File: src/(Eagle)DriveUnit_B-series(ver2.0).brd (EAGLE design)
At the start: 65.7 x 51 mm, 55 parts, among them IC1 A3921, SW1 TVAF06-A020B-R, SW2 TVAF06-A020B-R, SW3 THAF01-NC-R, SW4 SS-12D00G3

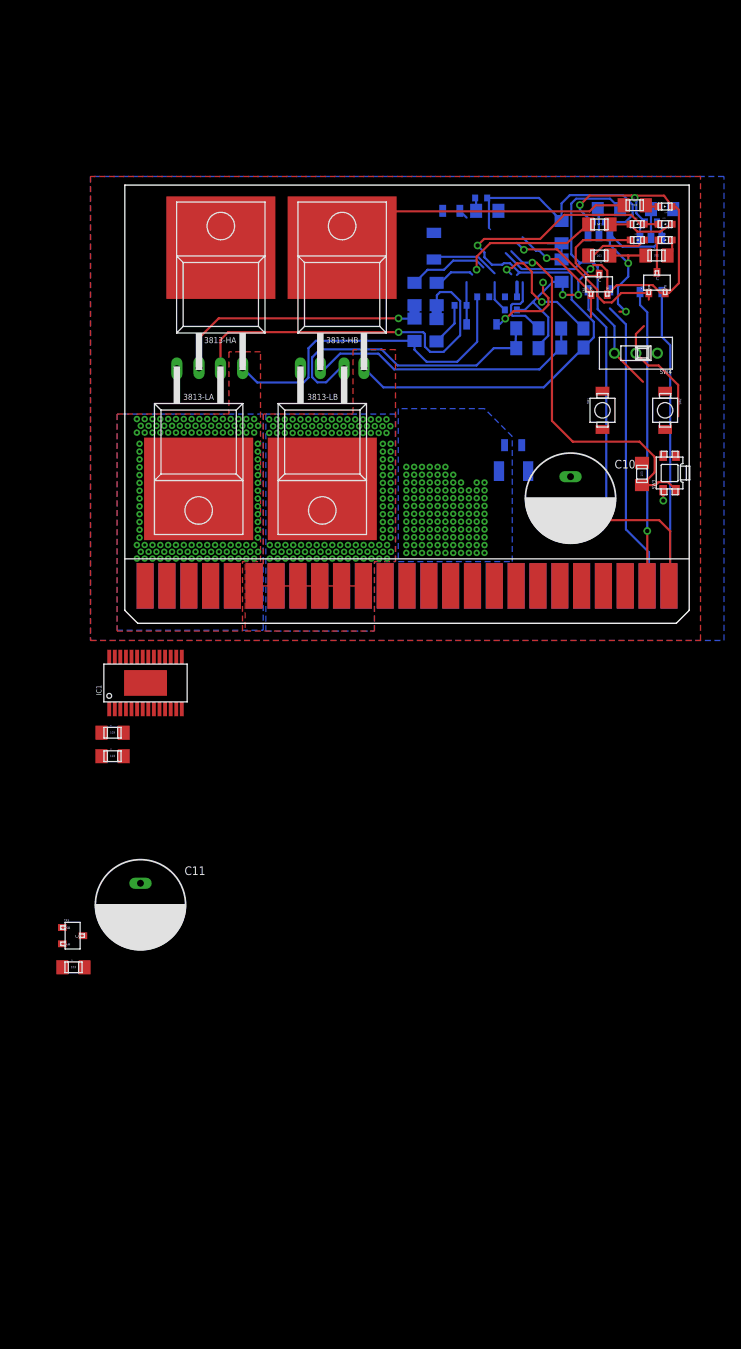
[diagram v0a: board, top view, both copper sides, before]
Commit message: 入力部分の追加
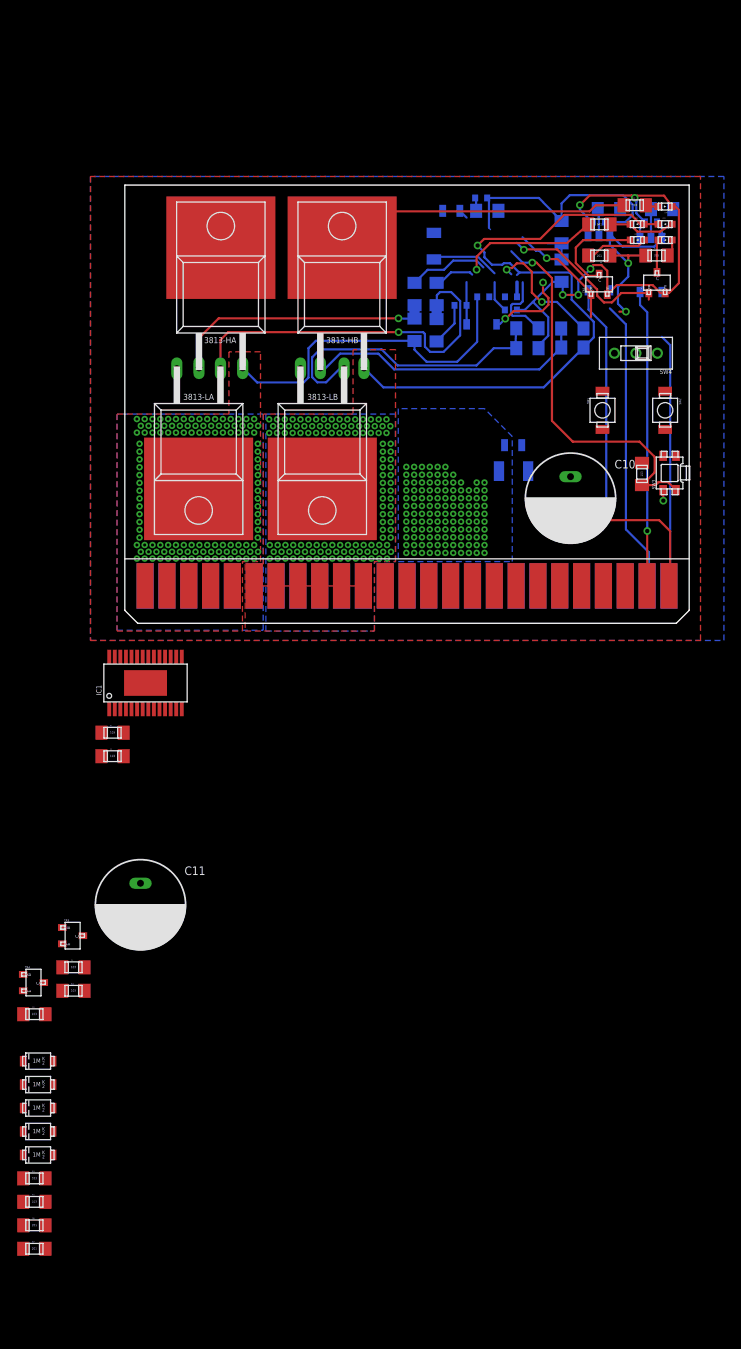
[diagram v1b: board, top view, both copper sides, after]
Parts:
- added D2, D3, D4, D5, D6: GS1010FL, GS1010FL:GS1010FL
- added R17, R23, R24, R25: RG2012, RG2012:RG2012
- added R26, R27: RG2012N-201-W-T1, RG2012N-201-W-T1:RG2012
- added TR4: 2SC3325, 2SC3325:2SC3325
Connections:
- new net LAP: D4.A, D5.A, R25.LEFT, R9.LEFT, SW4.C, TR3.B
- new net N$12: D3.A, R23.LEFT, TR4.C
- new net N$17: D4.C, R17.LEFT, R24.LEFT, SW1.RIGHT, TR4.B
- new net N$20: D5.C, D6.C, SW2.LEFT
- new net N$23: R26.LEFT, TLP1.1
- new net N$24: R27.LEFT, TLP2.1
- net DIR: now also D2.A, D2.C, D3.C, D6.A; no longer R9.LEFT, SW1.RIGHT, TR3.B
- net DIR_IN: now also R26.RIGHT; no longer TLP1.1
- net GND: now also R24.RIGHT, R25.RIGHT, SW2.RIGHT, SW4.R, TR4.E
- net PWM: no longer SW4.R
- net PWM_IN: now also R27.RIGHT; no longer TLP2.1
- net V5: now also R17.RIGHT, R23.RIGHT; no longer SW4.C
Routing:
- net PWM: track 41.4 -> 0.00 mm
- net V5: track 70.5 -> 56.9 mm
- net DIR_IN: track 34.7 -> 29.5 mm

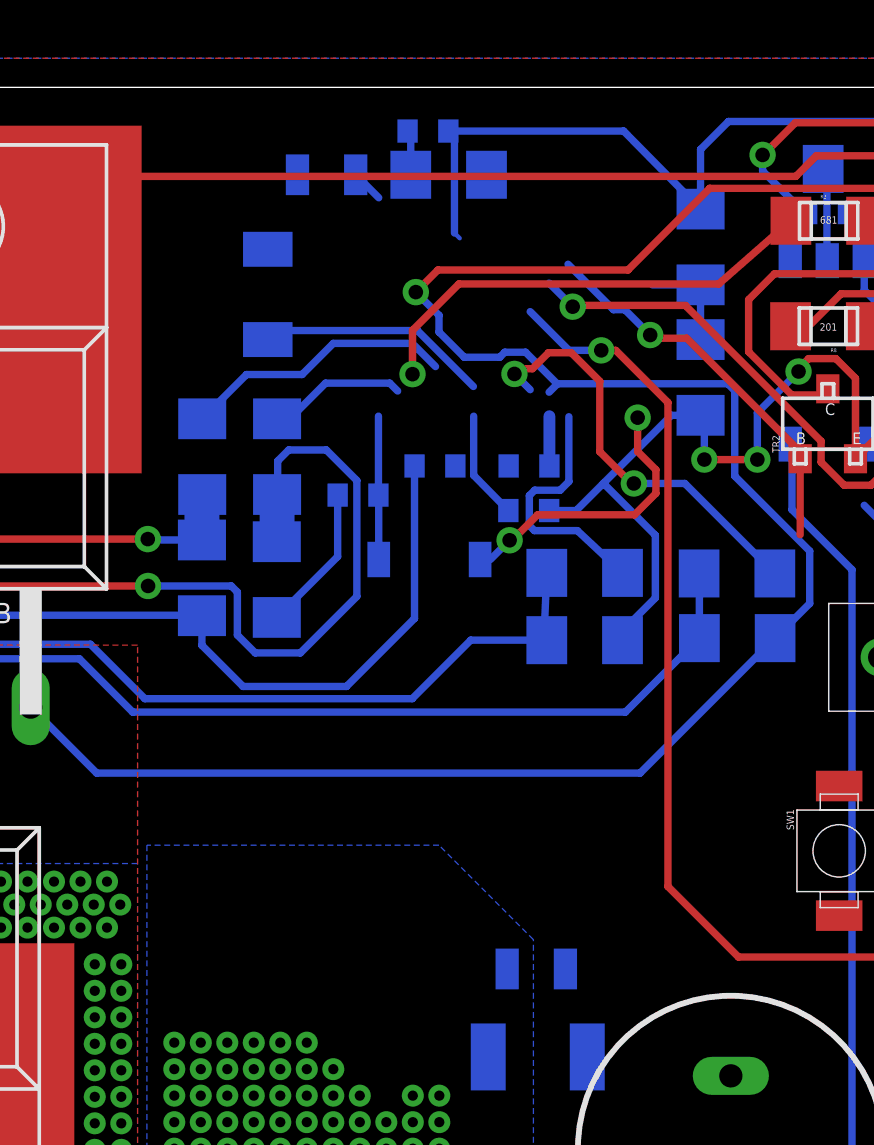
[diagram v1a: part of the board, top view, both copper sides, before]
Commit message: [fix]デッドタイムを100kΩ可変抵抗で調整できるように変更
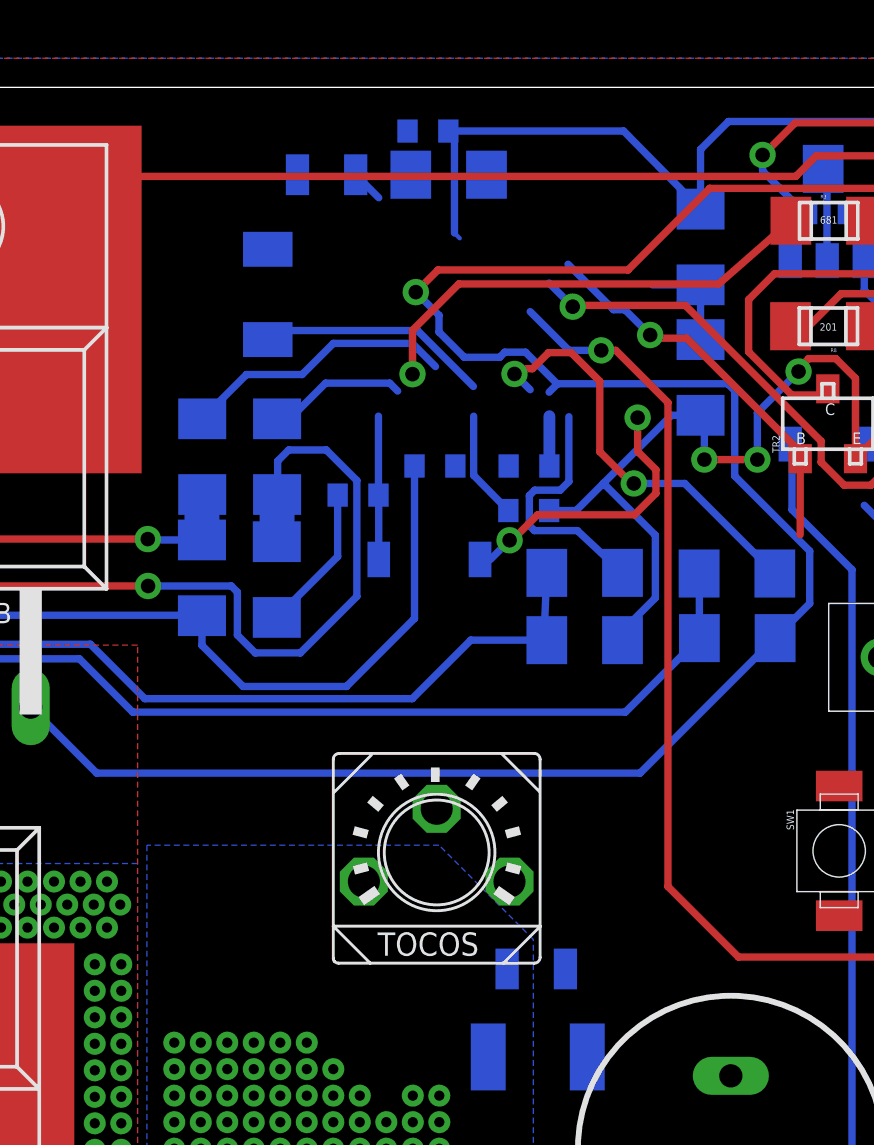
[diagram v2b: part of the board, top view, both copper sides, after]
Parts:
- added R28: 100k, GF063P B104K:GF063PB104K
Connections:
- new net N$16: R13.RIGHT, R28.CENTER, R28.RIGHT
- net GND: now also R28.LEFT; no longer R13.RIGHT
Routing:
- net GND: track 74.9 -> 72.9 mm
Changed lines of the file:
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@@
 <attribute name="NAME" x="-10.814" y="-72.038" size="0.127" layer="25"/>
 </element>
+<element name="R28" library="GF063P B104K" package="GF063PB104K" value="100k" x="38.22" y="20.93" smashed="yes"/>
 </elements>
 <signals>
@@
 <contactref element="R15" pad="LEFT"/>
 <contactref element="R18" pad="LEFT"/>
-<contactref element="R13" pad="RIGHT"/>
 <contactref element="R2" pad="RIGHT"/>
 <contactref element="SW3" pad="1"/>
@@
 <wire x1="53.91" y1="46.12" x2="53.91" y2="45.05" width="0.254" layer="16"/>
 <wire x1="40.77" y1="49.5" x2="40.88" y2="49.39" width="0.1524" layer="16"/>
-<wire x1="40.88" y1="49.39" x2="40.88" y2="48" width="0.254" layer="16"/>
-<wire x1="40.43" y1="47.55" x2="40.88" y2="48" width="0.254" layer="16"/>
 <wire x1="49.83" y1="39.74" x2="50.83" y2="39.74" width="0.254" layer="16"/>
 <wire x1="48.15" y1="32.02" x2="48.064046875" y2="32.255759375" width="0.254" layer="16"/>
@@
 <contactref element="C10" pad="C"/>
 <contactref element="C11" pad="C"/>
-<contactref element="SW2" pad="RIGHT"/>
-<contactref element="SW1" pad="LEFT"/>
 <contactref element="TR3" pad="E"/>
 <contactref element="TR4" pad="E"/>
@@
 <contactref element="R25" pad="RIGHT"/>
 <contactref element="SW4" pad="R"/>
-<wire x1="50.83" y1="39.74" x2="50.96" y2="39.61" width="0" layer="19" extent="16-16"/>
+<contactref element="SW2" pad="RIGHT"/>
+<contactref element="SW1" pad="LEFT"/>
+<contactref element="R28" pad="LEFT"/>
+<wire x1="35.97" y1="45.44" x2="40.77" y2="49.5" width="0" layer="19" extent="16-16"/>
+<wire x1="38.37" y1="37" x2="35.97" y2="45.44" width="0" layer="19" extent="16-16"/>
+<wire x1="45.63" y1="36.47" x2="38.37" y2="37" width="0" layer="19" extent="16-16"/>
+<wire x1="50.96" y1="39.61" x2="50.83" y2="39.74" width="0" layer="19" extent="16-16"/>
 <wire x1="56.98" y1="31.43" x2="56.15" y2="38.25" width="0" layer="19" extent="1-1"/>
 <wire x1="55.59" y1="27.01" x2="56.98" y2="31.43" width="0" layer="19" extent="1-1"/>
-<wire x1="38.37" y1="37" x2="45.63" y2="36.47" width="0" layer="19" extent="16-16"/>
 <wire x1="62.88" y1="22.56" x2="55.59" y2="27.01" width="0" layer="19" extent="1-1"/>
 <wire x1="62.65" y1="15.49" x2="62.88" y2="22.56" width="0" layer="19" extent="1-1"/>
-<wire x1="35.97" y1="45.44" x2="38.37" y2="37" width="0" layer="19" extent="16-16"/>
-<wire x1="40.43" y1="47.55" x2="35.97" y2="45.44" width="0" layer="19" extent="16-16"/>
 <wire x1="58.24" y1="4.35" x2="62.67" y2="14.27" width="0" layer="19" extent="16-16"/>
 <wire x1="55.7" y1="4.35" x2="58.24" y2="4.35" width="0" layer="19" extent="16-16"/>
@@
 <wire x1="-9.23" y1="-64.61" x2="-11.83" y2="-42.77" width="0" layer="19" extent="1-1"/>
 <wire x1="-9.23" y1="-67.34" x2="-9.23" y2="-64.61" width="0" layer="19" extent="1-1"/>
+<wire x1="39.27" y1="23.73" x2="-9.23" y2="-67.34" width="0" layer="19" extent="1-1"/>
 </signal>
 <signal name="RESET">
@@
 <wire x1="6.63" y1="-3.9" x2="36.99" y2="48" width="0" layer="19" extent="1-16"/>
 </signal>
-<signal name="N$16">
-<contactref element="IC1" pad="27"/>
-<contactref element="R13" pad="LEFT"/>
-<wire x1="-1.17" y1="-3.9" x2="43.48" y2="48" width="0" layer="19" extent="1-16"/>
-</signal>
 <signal name="N$3">
 <contactref element="C7" pad="P$1"/>
@@
 <wire x1="-11.83" y1="-67.34" x2="-8.35" y2="-56.42" width="0" layer="19" extent="1-1"/>
 </signal>
+<signal name="N$19">
+<contactref element="R13" pad="LEFT"/>
+<contactref element="IC1" pad="27"/>
+<wire x1="-1.17" y1="-3.9" x2="43.48" y2="48" width="0" layer="19" extent="1-16"/>
+</signal>
+<signal name="N$16">
+<contactref element="R28" pad="RIGHT"/>
+<contactref element="R28" pad="CENTER"/>
+<contactref element="R13" pad="RIGHT"/>
+<wire x1="41.77" y1="26.23" x2="40.88" y2="48" width="0" layer="19" extent="16-16"/>
+<wire x1="44.27" y1="23.73" x2="41.77" y2="26.23" width="0" layer="19" extent="1-1"/>
+</signal>
 </signals>

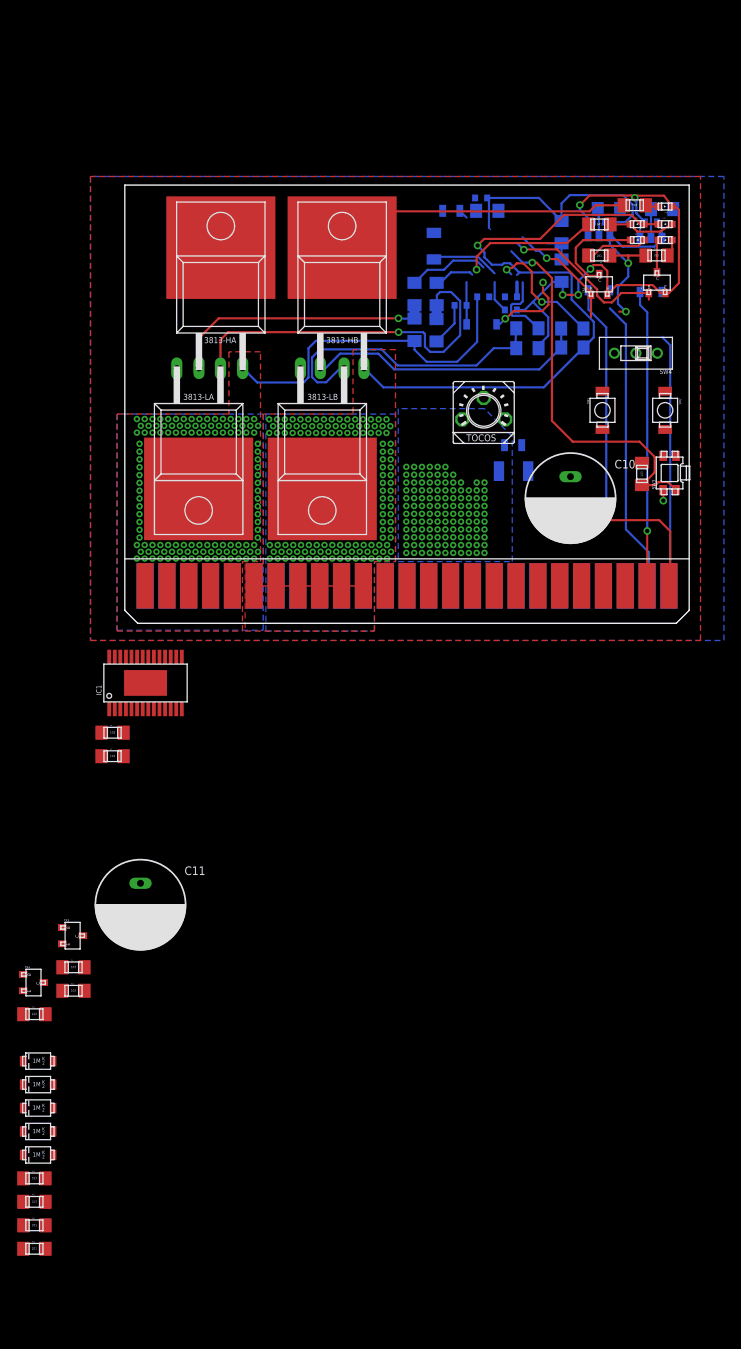
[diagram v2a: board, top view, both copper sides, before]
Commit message: [add]電流センサ周りの配線_1
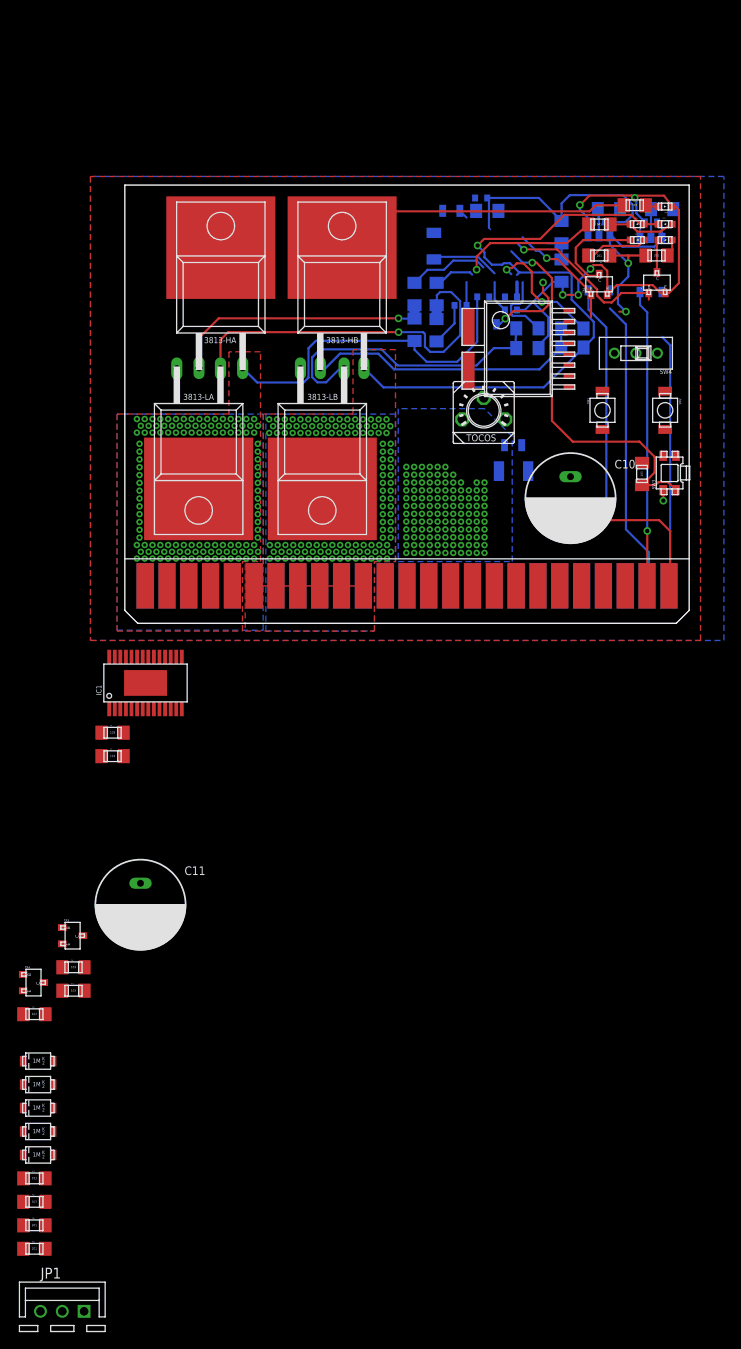
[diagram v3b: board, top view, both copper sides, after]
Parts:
- added IC2: CZ3A07, CZ3A07:CZ3A07
- added JP1: (no value), con-jst-xh:B3B-XH
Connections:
- new net VOUT: JP1.2
- net GND_IN: now also IC2.OCD2, IC2.REF2, IC2.VSS1, JP1.1
- net SA: now also IC2.IP
- net SB: now also IC2.IN
- net VCC_IN: now also JP1.3
